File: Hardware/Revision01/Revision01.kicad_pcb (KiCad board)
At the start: 4 copper layers, 100 x 110.1 mm, 101 parts, among them J10 StrainConn, J11 StrainConn, J12 StrainConn, J14 Conn_01x05, J2 Conn_01x02, J3 Conn_01x02, J4 Battery connector, J5 StrainConn, J6 StrainConn, J7 StrainConn, J8 StrainConn, J9 StrainConn, Q1 PMOS, Q2 NMOS, Q3 PMOS, SW1 ON/OFF_SW_SPST_LED, U1 NUCLEO-L476RG, U2 MRF89XAM9AT-I/RM, U3 MPU-6500

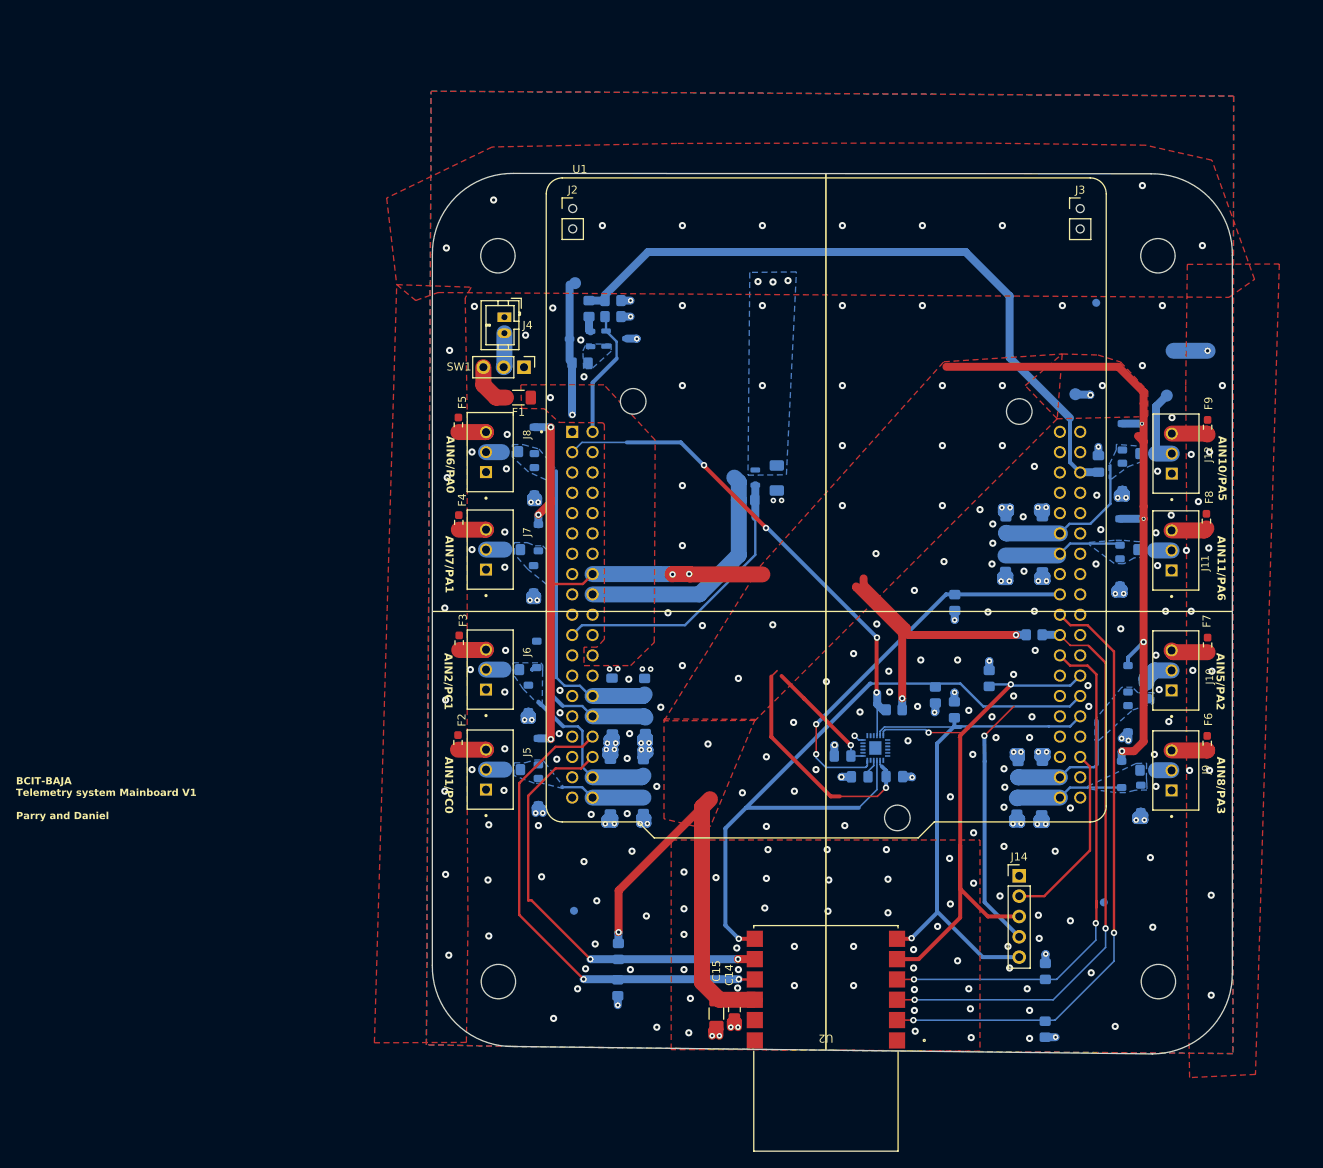
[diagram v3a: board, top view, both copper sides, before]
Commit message: PART A schematic - debugging headers added, DRC has been checked, initial gerberfiles created(not checked)
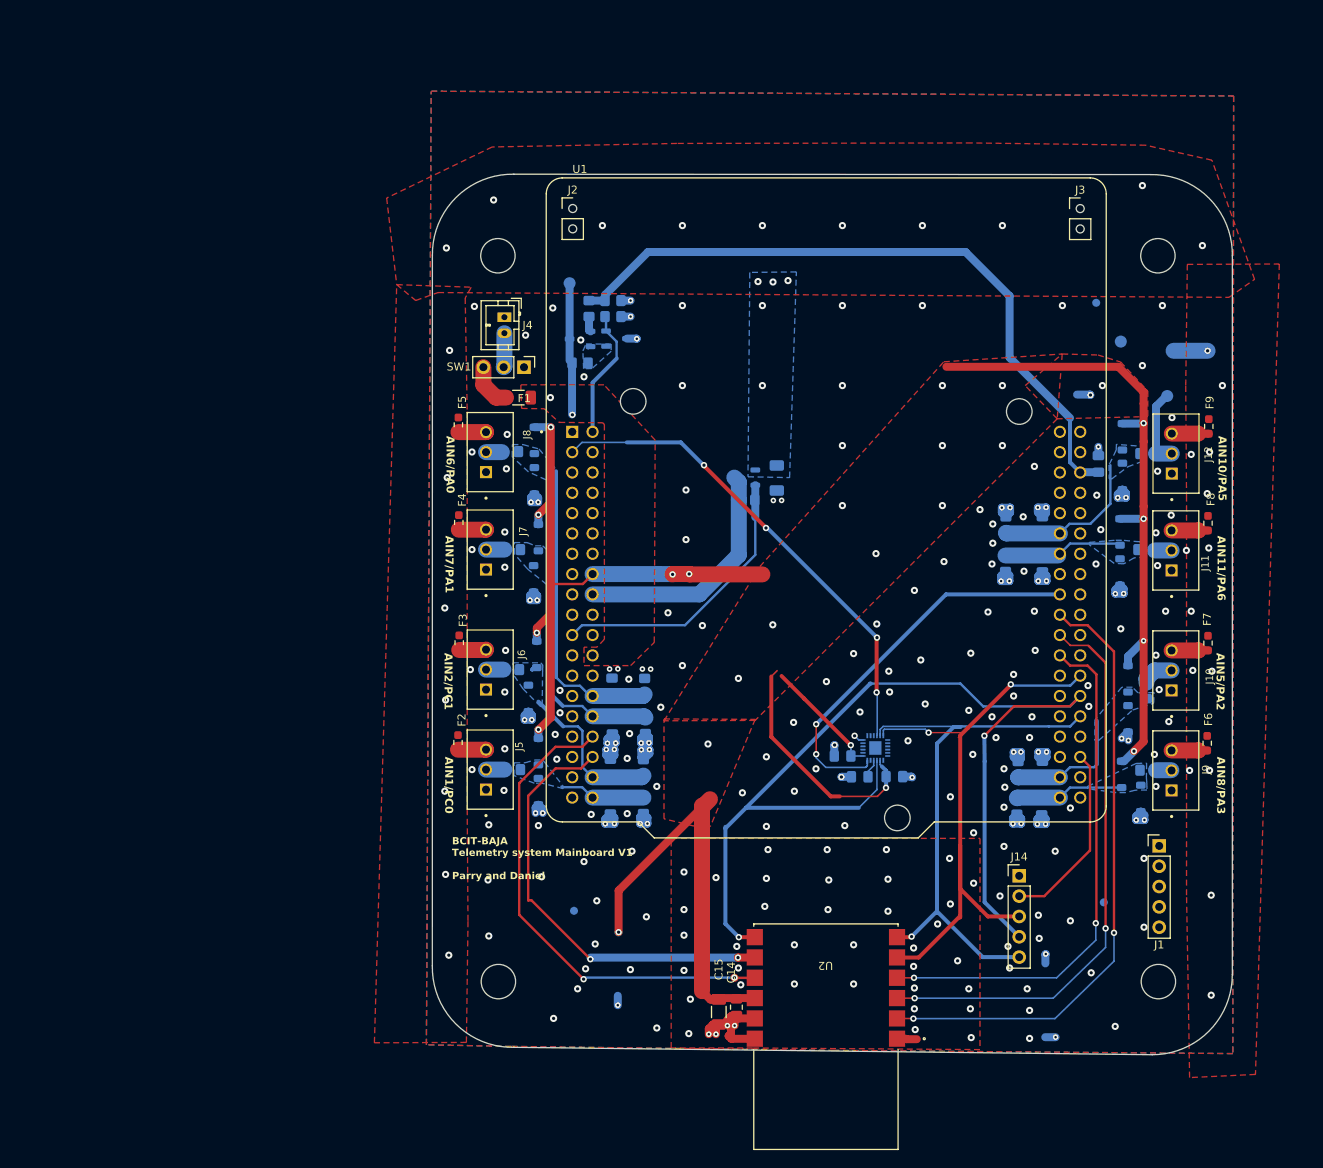
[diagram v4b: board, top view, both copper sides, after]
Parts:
- removed +VStrain, +V_batt, AIN10, GND: TestPoint, TestPoint:TestPoint_Pad_D1.5mm
- removed R33, R34, R35, R36, R37, R38, R39, R40, R41, R42: 10K +-1%, Resistor_SMD:R_0805_2012Metric_Pad1.20x1.40mm_HandSolder
- added J1: Conn_01x05, Connector_PinHeader_2.54mm:PinHeader_1x05_P2.54mm_Vertical, F.Cu at (201.9, 126.7)
- added TP10: TestPoint, TestPoint:TestPoint_Pad_D1.5mm, B.Cu at (203.7, 64.9)
- added TP3: TestPoint, TestPoint:TestPoint_Pad_D1.5mm, B.Cu at (128.2, 56.4)
- added TP8: TestPoint, TestPoint:TestPoint_Pad_D1.5mm, B.Cu at (197.1, 63.7)
- added TP9: TestPoint, TestPoint:TestPoint_Pad_D1.5mm, B.Cu at (202.9, 70.5)
- moved C14 0.39 mm to (149.0, 146.9)
- moved C15 0.36 mm to (146.8, 147.5)
- moved F8 0.33 mm to (208.0, 86.4)
- moved F7 0.23 mm to (208.0, 101.4)
- moved U2 0.21 mm to (160.2, 150.6)
- moved F9 0.18 mm to (208.1, 74.3)
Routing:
- net +3.3V: track 299.3 -> 259.6 mm, vias 14 -> 13
- net /PB14_SPI2_MISO: track 123.2 -> 132.0 mm
- net GND: track 104.8 -> 109.8 mm, vias 282 -> 278
- net /MPU_CS_GPIO: track 63.9 -> 61.1 mm
- net /PB15_SPI2_MOSI: track 81.4 -> 78.7 mm
- net /ANT_CSCON_GPIO: track 73.7 -> 71.4 mm
- net /ANT_IRQ0_GPIO: track 66.5 -> 65.5 mm
- net /PB13_SPI2_SCK: track 78.5 -> 77.6 mm
- net +V_batt: track 17.2 -> 16.7 mm
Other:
- board text added: "+VStrain"
- board text added: "AIN10"
- board text added: "GND"

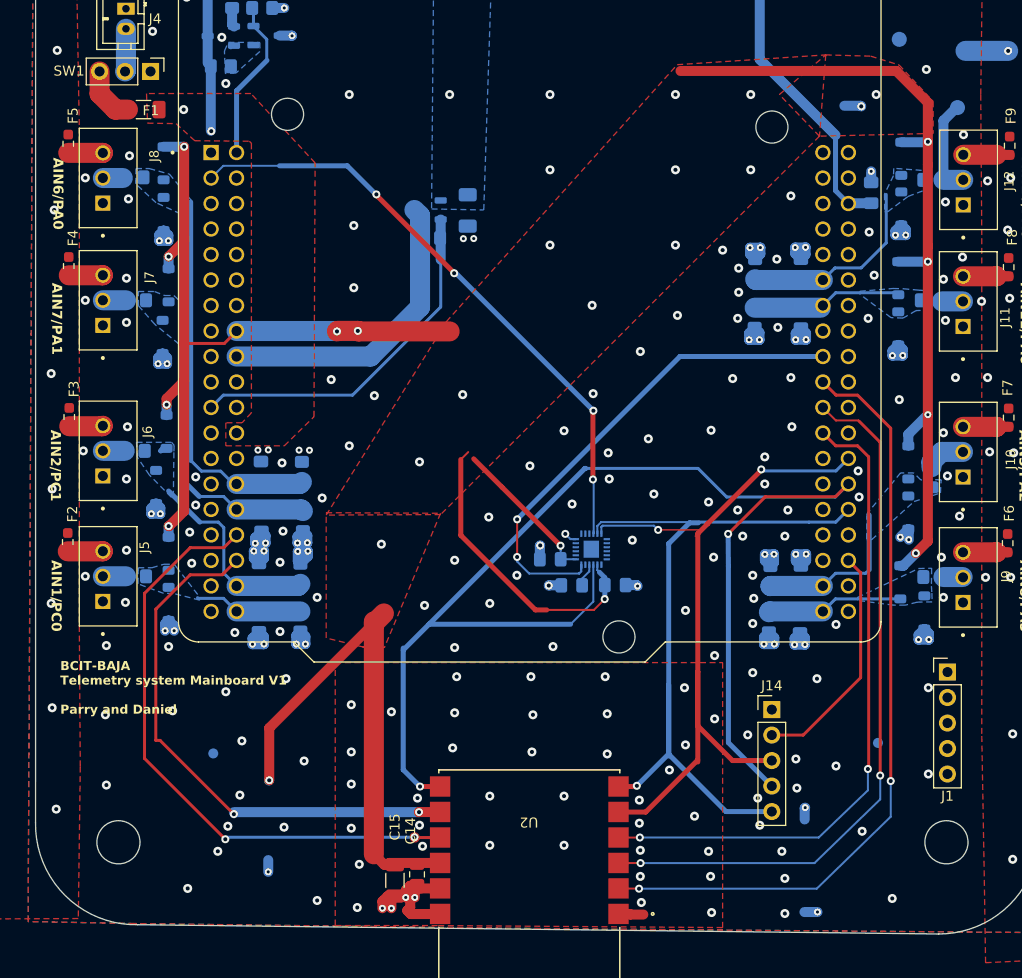
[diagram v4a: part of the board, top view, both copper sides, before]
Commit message: PART A - sent to manufacturer for review
ALL NUCLEO PINS configured/verified ON STM32IDE,
verified battery INPUT WORKS - note 5V rail is 3.9V utilizing 10V battery
Removed floating traces
Improved silkscreen
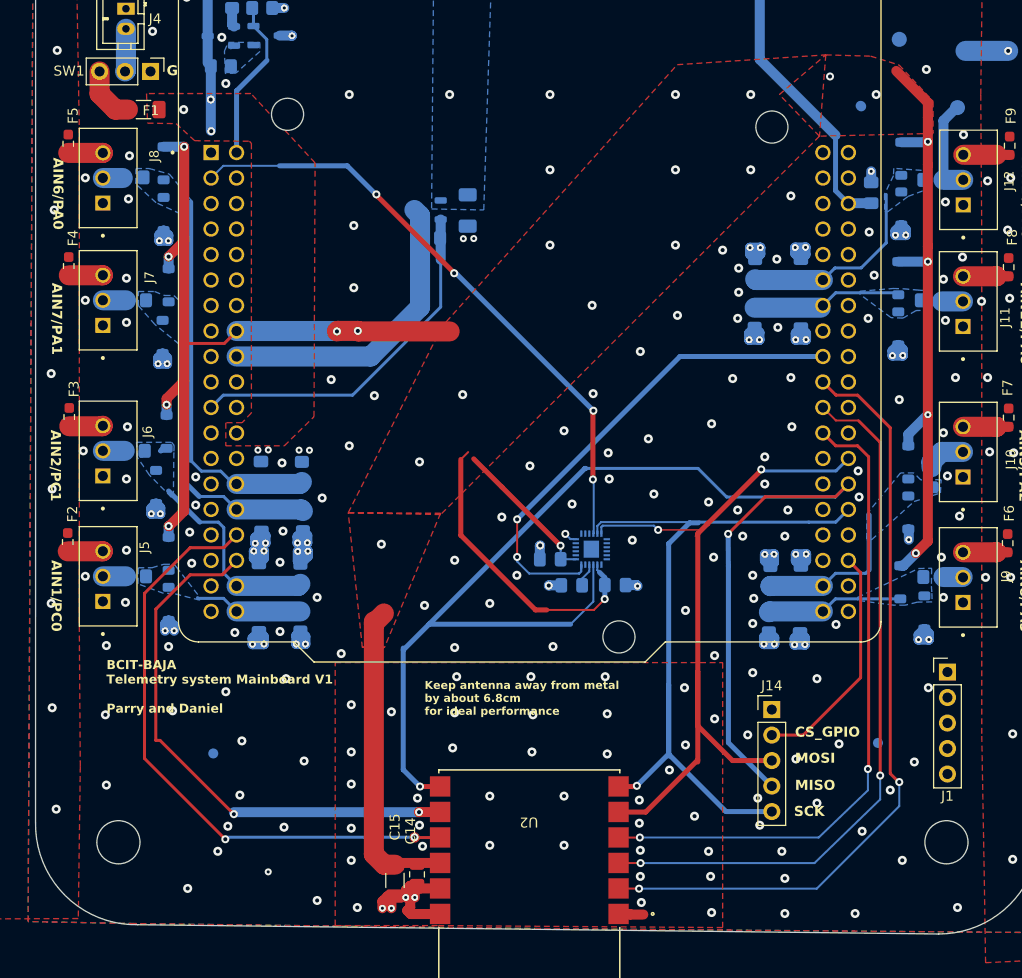
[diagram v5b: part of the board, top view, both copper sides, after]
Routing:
- net +3.3V: track 259.6 -> 217.3 mm, vias 13 -> 12
- net GND: track 109.8 -> 103.4 mm, vias 278 -> 279
- net /ANT_RESET_ANT_GPIO: track 77.4 -> 78.1 mm
- net +V_batt: vias 1 -> 2
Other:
- rule pad_to_mask_clearance: 0.08 -> 0
- board text added: "CS_GPIO"
- board text added: "G"
- board text added: "Keep antenna away from metal by about 6.8cm for ideal performance"
- board text added: "MISO"
- board text added: "MOSI"
- board text added: "SCK"

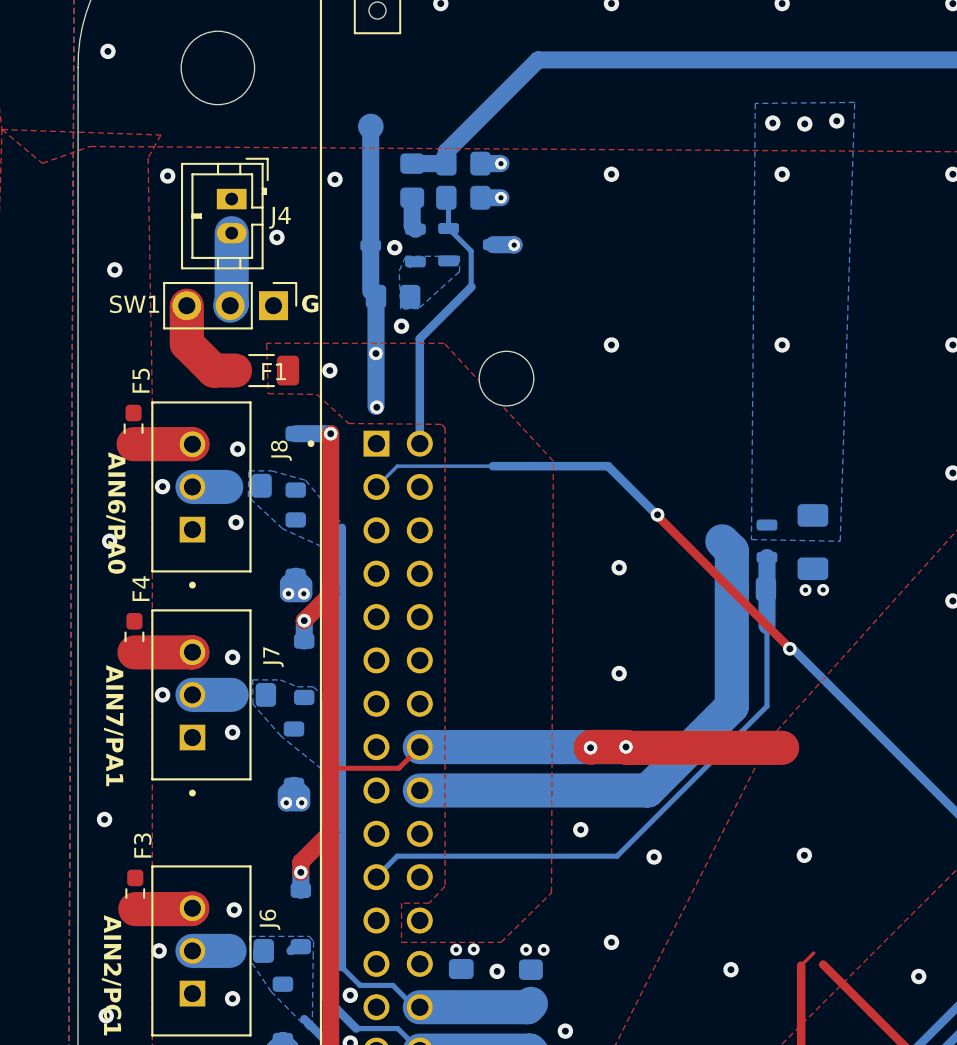
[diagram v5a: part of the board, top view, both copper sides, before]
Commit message: REWIRING SCHEMATIC OVER HEAT CONCERN - picked and wired buck-converter - started FMEA analysis
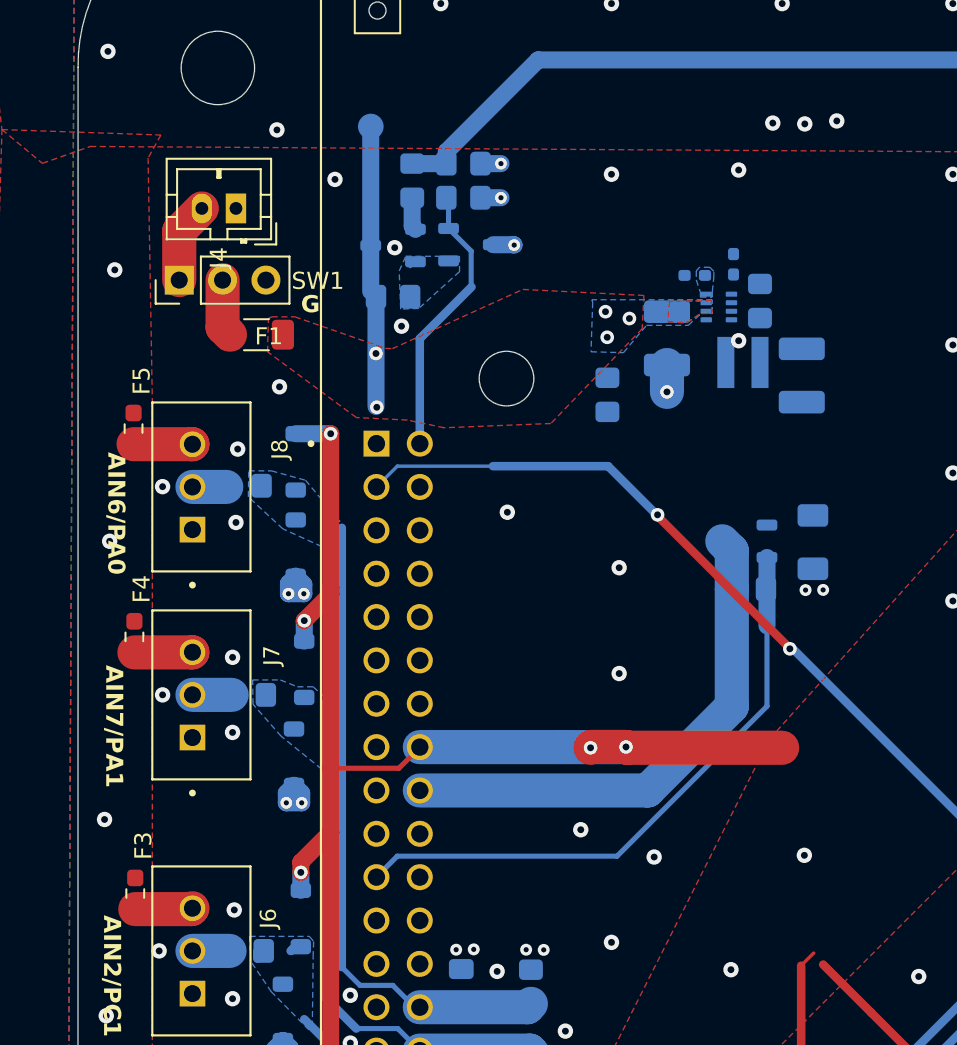
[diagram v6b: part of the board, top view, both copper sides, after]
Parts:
- added C20: 22uF, Capacitor_SMD:C_1210_3225Metric_Pad1.33x2.70mm_HandSolder, B.Cu at (145.5, 68.8)
- added C21: 22uF, Capacitor_SMD:C_1210_3225Metric_Pad1.33x2.70mm_HandSolder, B.Cu at (153.4, 71.0)
- added L1: 2.2uH, VLS3012CX_2R2M_1:IND_VLS3012CX-2R2M-1, B.Cu at (150.0, 70.2)
- added R33: 53.2K, Resistor_SMD:R_0402_1005Metric_Pad0.72x0.64mm_HandSolder, B.Cu at (147.2, 65.1)
- added R34: 100K, Resistor_SMD:R_0805_2012Metric_Pad1.20x1.40mm_HandSolder, B.Cu at (151.0, 66.6)
- added R35: 124K, Resistor_SMD:R_0402_1005Metric_Pad0.72x0.64mm_HandSolder, B.Cu at (149.4, 64.5)
- added R36: 0, Resistor_SMD:R_0805_2012Metric_Pad1.20x1.40mm_HandSolder, B.Cu at (142.0, 72.1)
- added U5: TPS629203QDRLRQ1, Package_TO_SOT_SMD:SOT-583-8, B.Cu at (148.6, 67.0)
- moved SW1 5.73 mm to (117.0, 65.4), turned to 90 degrees
- moved F1 2.12 mm to (121.5, 68.6)
- moved J4 0.60 mm to (120.3, 61.2), turned to 180 degrees
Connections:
- SW1 pad 1: GND -> Net-(BT1-+)
- SW1 pad 2: Net-(BT1-+) -> Net-(SW1-A)
- SW1 pad 3: Net-(SW1-A) -> GND
- U1 pad CN7_24: +V_batt -> +Vin_5.5V
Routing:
- net Net-(SW1-A): track 5.70 -> 3.38 mm
- net GND: track 103.4 -> 105.0 mm
- net +V_batt: vias 2 -> 5
- added copper zone on B.Cu, net +V_batt
- added copper zone on B.Cu, net Net-(U5-MODE/S-CONF)
- removed copper zone on B.Cu, net /Application/+StrainV
